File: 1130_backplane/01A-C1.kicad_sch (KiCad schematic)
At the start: 86 parts

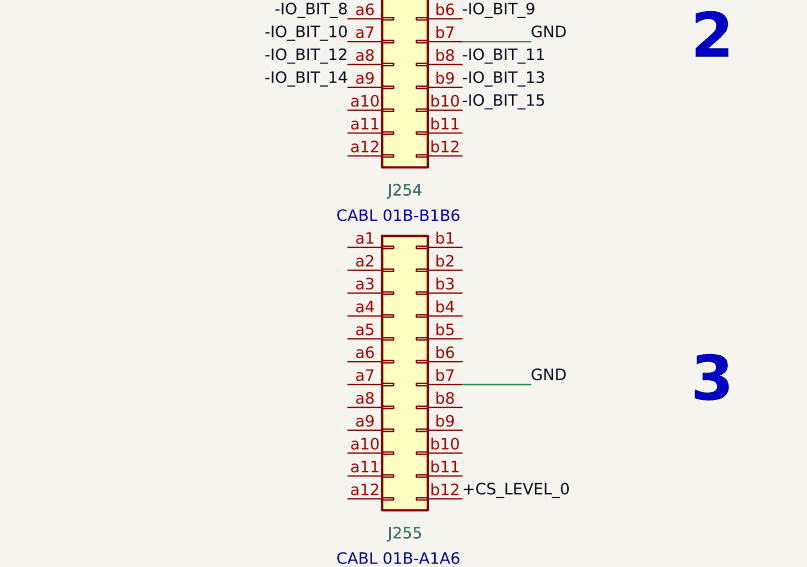
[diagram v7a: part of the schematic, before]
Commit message: Finish page RA101-RA171
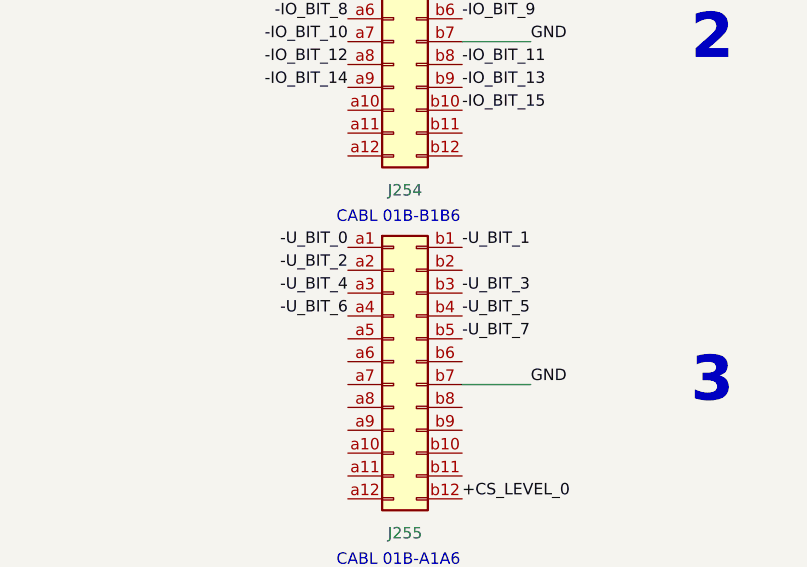
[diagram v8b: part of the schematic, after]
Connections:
- net -U_BIT_0: now also J254.a1 (Pin_a1)
- net -U_BIT_1: now also J254.b1 (Pin_b1)
- net -U_BIT_2: now also J254.a2 (Pin_a2)
- net -U_BIT_3: now also J254.b3 (Pin_b3)
- net -U_BIT_4: now also J254.a3 (Pin_a3)
- net -U_BIT_5: now also J254.b4 (Pin_b4)
- net -U_BIT_6: now also J254.a4 (Pin_a4)
- net -U_BIT_7: now also J254.b5 (Pin_b5)
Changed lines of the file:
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@@
+    (effects (font (size 1.27 1.27)) (justify right bottom))
+  )
+  (label "-U_BIT_2" (at 795.02 144.78 180)
     (effects (font (size 1.27 1.27)) (justify right bottom))
   )
@@
     (effects (font (size 1.27 1.27)) (justify right bottom))
   )
+  (label "-U_BIT_1" (at 807.72 142.24 0)
+    (effects (font (size 1.27 1.27)) (justify left bottom))
+  )
   (label "-3V" (at 342.9 114.3 180)
     (effects (font (size 1.27 1.27)) (justify right bottom))
@@
     (effects (font (size 1.27 1.27)) (justify right bottom))
   )
+  (label "-U_BIT_5" (at 807.72 149.86 0)
+    (effects (font (size 1.27 1.27)) (justify left bottom))
+  )
   (label "+3V" (at 307.34 297.18 0)
     (effects (font (size 1.27 1.27)) (justify left bottom))
@@
     (effects (font (size 1.27 1.27)) (justify left bottom))
   )
+  (label "-U_BIT_4" (at 795.02 147.32 180)
+    (effects (font (size 1.27 1.27)) (justify right bottom))
+  )
   (label "GND" (at 497.84 271.78 0)
     (effects (font (size 1.27 1.27)) (justify left bottom))
@@
     (effects (font (size 1.27 1.27)) (justify left bottom))
   )
+  (label "-U_BIT_3" (at 807.72 147.32 0)
+    (effects (font (size 1.27 1.27)) (justify left bottom))
+  )
   (label "+U_REG_5_PWR" (at 426.72 167.64 0)
     (effects (font (size 1.27 1.27)) (justify left bottom))
@@
     (effects (font (size 1.27 1.27)) (justify right bottom))
   )
+  (label "-U_BIT_6" (at 795.02 149.86 180)
+    (effects (font (size 1.27 1.27)) (justify right bottom))
+  )
   (label "+3V" (at 180.34 259.08 0)
     (effects (font (size 1.27 1.27)) (justify left bottom))
@@
     (effects (font (size 1.27 1.27)) (justify right bottom))
   )
+  (label "-U_BIT_7" (at 807.72 152.4 0)
+    (effects (font (size 1.27 1.27)) (justify left bottom))
+  )
   (label "+6V" (at 25.4 165.1 180)
     (effects (font (size 1.27 1.27)) (justify right bottom))
@@
     (effects (font (size 1.27 1.27)) (justify right bottom))
   )
+  (label "-U_BIT_0" (at 795.02 142.24 180)
+    (effects (font (size 1.27 1.27)) (justify right bottom))
+  )
